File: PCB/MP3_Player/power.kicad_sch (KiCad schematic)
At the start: 18 parts, among them J5 BAT Connector, SW1 Power SW, U2 AP2112K-3.3, U3 BQ24075RGTR, U5 MAX17048G

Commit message: Minor Schematic Changes
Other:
- note added: "GND Test point"
- moved on the sheet: BT1, TP4
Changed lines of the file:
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@@
 	)
 	(rectangle
-		(start 114.3 139.7)
-		(end 129.54 151.13)
+		(start 49.53 152.4)
+		(end 64.77 163.83)
 		(stroke
 			(width 0)
@@
 	(text "Battery BOM Placeholder"
 		(exclude_from_sim no)
-		(at 124.46 154.432 0)
+		(at 57.658 167.386 0)
 		(effects
 			(font
@@
 	(text "For ERC\nIgnore"
 		(exclude_from_sim no)
-		(at 50.546 130.81 0)
+		(at 89.154 130.81 0)
 		(effects
 			(font
@@
 		)
 	)
+	(text "GND Test \npoint"
+		(exclude_from_sim no)
+		(at 108.966 130.81 0)
+		(effects
+			(font
+				(size 1.27 1.27)
+			)
+		)
+	)
 	(text "Power Switch"
 		(exclude_from_sim no)
@@
 	)
 	(no_connect
-		(at 125.73 143.51)
+		(at 60.96 156.21)
 	)
 	(no_connect
@@
 	)
 	(no_connect
-		(at 118.11 143.51)
+		(at 53.34 156.21)
 	)
 	(no_connect
@@
 	(wire
 		(pts
-			(xy 41.91 129.54) (xy 41.91 132.08)
+			(xy 95.25 129.54) (xy 95.25 132.08)
 		)
 		(stroke
@@
 	(wire
 		(pts
-			(xy 101.6 125.73) (xy 101.6 127)
+			(xy 102.87 130.81) (xy 102.87 132.08)
 		)
 		(stroke
@@
 	(symbol
 		(lib_id "power:GND")
-		(at 101.6 127 0)
+		(at 102.87 132.08 0)
 		(unit 1)
 		(body_style 1)
@@
 		(fields_autoplaced yes)
 		(property "Reference" "#PWR057"
-			(at 101.6 133.35 0)
+			(at 102.87 138.43 0)
 			(hide yes)
 			(show_name no)
@@
 		)
 		(property "Value" "GND"
-			(at 101.6 132.08 0)
+			(at 102.87 137.16 0)
 			(hide yes)
 			(show_name no)
@@
 		)
 		(property "Footprint" ""
-			(at 101.6 127 0)
+			(at 102.87 132.08 0)
 			(hide yes)
 			(show_name no)
@@
 		)
 		(property "Datasheet" ""
-			(at 101.6 127 0)
+			(at 102.87 132.08 0)
 			(hide yes)
 			(show_name no)
@@
 		)
 		(property "Description" "Power symbol creates a global label with name \"GND\" , ground"
-			(at 101.6 127 0)
+			(at 102.87 132.08 0)
 			(hide yes)
 			(show_name no)
@@
 	(symbol
 		(lib_id "power:PWR_FLAG")
-		(at 41.91 129.54 0)
+		(at 95.25 129.54 0)
 		(unit 1)
 		(body_style 1)
@@
 		(fields_autoplaced yes)
 		(property "Reference" "#FLG01"
-			(at 41.91 127.635 0)
+			(at 95.25 127.635 0)
 			(hide yes)
 			(show_name no)
@@
 		)
 		(property "Value" "PWR_FLAG"
-			(at 41.91 124.46 0)
+			(at 95.25 124.46 0)
 			(show_name no)
 			(do_not_autoplace no)
@@
 		)
 		(property "Footprint" ""
-			(at 41.91 129.54 0)
+			(at 95.25 129.54 0)
 			(hide yes)
 			(show_name no)
@@
 		)
 		(property "Datasheet" ""
-			(at 41.91 129.54 0)
+			(at 95.25 129.54 0)
 			(hide yes)
 			(show_name no)
@@
 		)
 		(property "Description" "Special symbol for telling ERC where power comes from"
-			(at 41.91 129.54 0)
+			(at 95.25 129.54 0)
 			(hide yes)
 			(show_name no)
@@
 	(symbol
 		(lib_id "Device:Battery_Cell")
-		(at 123.19 143.51 90)
+		(at 58.42 156.21 90)
 		(unit 1)
 		(body_style 1)
@@
 		(dnp no)
 		(property "Reference" "BT1"
-			(at 122.428 147.32 90)
+			(at 57.658 160.02 90)
 			(show_name no)
 			(do_not_autoplace no)
@@
 		)
 		(property "Value" "Battery_Cell"
-			(at 122.3645 148.844 90)
+			(at 57.5945 161.544 90)
 			(show_name no)
 			(do_not_autoplace no)
@@
 		)
 		(property "Footprint" ""
-			(at 121.666 143.51 90)
+			(at 56.896 156.21 90)
 			(hide yes)
 			(show_name no)
@@
 		)
 		(property "Datasheet" ""
-			(at 121.666 143.51 90)
+			(at 56.896 156.21 90)
 			(hide yes)
 			(show_name no)
@@
 		)
 		(property "Description" "Single-cell battery"
-			(at 123.19 143.51 0)
+			(at 58.42 156.21 0)
 			(hide yes)
 			(show_name no)
@@
 		)
 		(property "Sim.Device" "V"
-			(at 123.19 143.51 0)
+			(at 58.42 156.21 0)
 			(hide yes)
 			(show_name no)
@@
 		)
 		(property "Sim.Type" "DC"
-			(at 123.19 143.51 0)
+			(at 58.42 156.21 0)
 			(hide yes)
 			(show_name no)
@@
 		)
 		(property "Sim.Pins" "1=+ 2=-"
-			(at 123.19 143.51 0)
+			(at 58.42 156.21 0)
 			(hide yes)
 			(show_name no)
@@
 		)
 		(property "Mfr. Part Number" ""
-			(at 123.19 143.51 90)
+			(at 58.42 156.21 90)
 			(hide yes)
 			(show_name no)
@@
 	(symbol
 		(lib_id "power:GND")
-		(at 41.91 132.08 0)
+		(at 95.25 132.08 0)
 		(unit 1)
 		(body_style 1)
@@
 		(fields_autoplaced yes)
 		(property "Reference" "#PWR074"
-			(at 41.91 138.43 0)
+			(at 95.25 138.43 0)
 			(hide yes)
 			(show_name no)
@@
 		)
 		(property "Value" "GND"
-			(at 41.91 137.16 0)
+			(at 95.25 137.16 0)
 			(hide yes)
 			(show_name no)
@@
 		)
 		(property "Footprint" ""
-			(at 41.91 132.08 0)
+			(at 95.25 132.08 0)
 			(hide yes)
 			(show_name no)
@@
 		)
 		(property "Datasheet" ""
-			(at 41.91 132.08 0)
+			(at 95.25 132.08 0)
 			(hide yes)
 			(show_name no)
@@
 		)
 		(property "Description" "Power symbol creates a global label with name \"GND\" , ground"
-			(at 41.91 132.08 0)
+			(at 95.25 132.08 0)
 			(hide yes)
 			(show_name no)
@@
 	(symbol
 		(lib_id "Connector:TestPoint")
-		(at 101.6 125.73 0)
+		(at 102.87 130.81 0)
 		(unit 1)
 		(body_style 1)
@@
 		(dnp no)
 		(property "Reference" "TP4"
-			(at 105.283 121.285 0)
+			(at 103.124 122.428 0)
 			(show_name no)
 			(do_not_autoplace no)
@@
 		)
 		(property "Value" "GND"
-			(at 105.283 123.825 0)
+			(at 103.124 124.968 0)
 			(show_name no)
 			(do_not_autoplace no)
@@
 		)
 		(property "Footprint" "Relay_THT:Relay_DPDT_Schrack-RT2-FormC_RM5mm"
-			(at 106.68 125.73 0)
+			(at 107.95 130.81 0)
 			(hide yes)
 			(show_name no)
@@
 		)
 		(property "Datasheet" ""
-			(at 106.68 125.73 0)
+			(at 107.95 130.81 0)
 			(hide yes)
 			(show_name no)
@@
 		)
 		(property "Description" "test point"
-			(at 101.6 125.73 0)
+			(at 102.87 130.81 0)
 			(hide yes)
 			(show_name no)

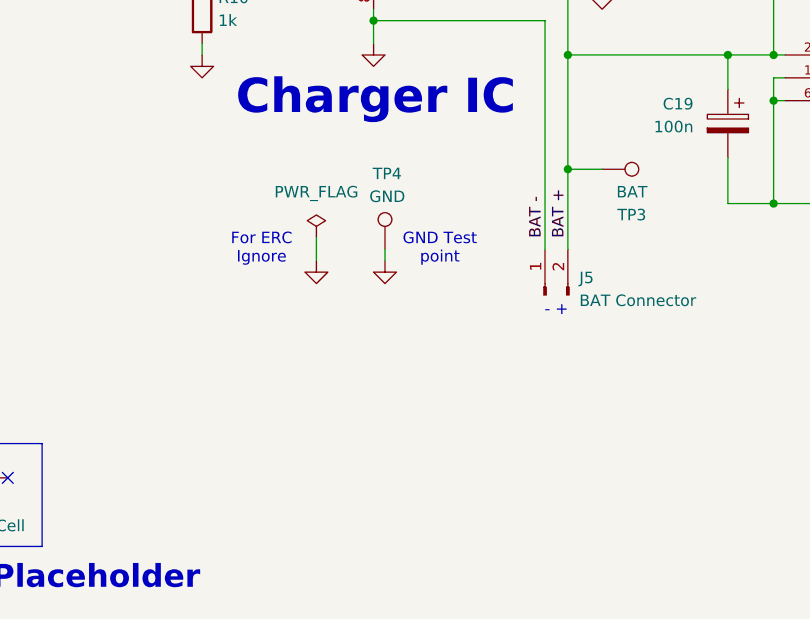
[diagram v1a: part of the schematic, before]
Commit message: Visual Schematic Corrections
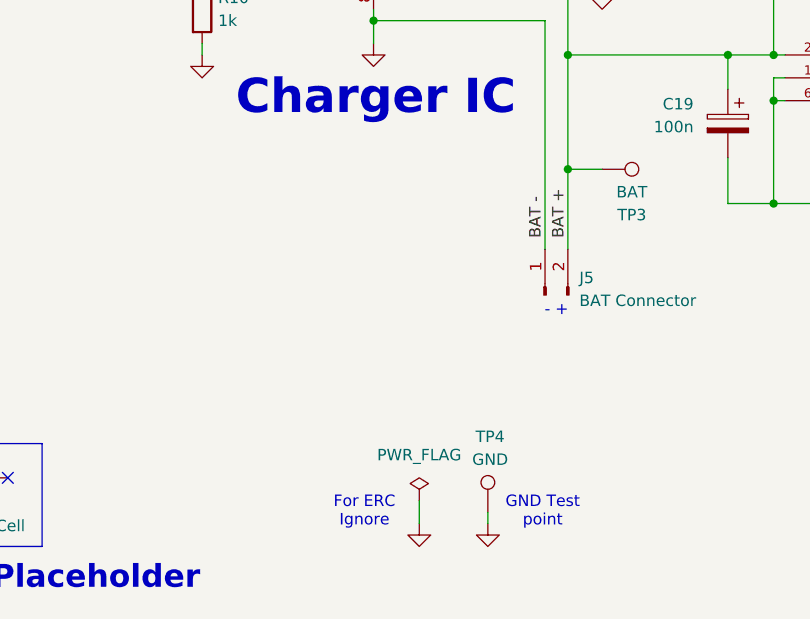
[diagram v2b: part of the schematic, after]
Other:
- moved on the sheet: TP4
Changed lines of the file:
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@@
 	(text "For ERC\nIgnore"
 		(exclude_from_sim no)
-		(at 89.154 130.81 0)
+		(at 100.584 160.02 0)
 		(effects
 			(font
@@
 	(text "GND Test \npoint"
 		(exclude_from_sim no)
-		(at 108.966 130.81 0)
+		(at 120.396 160.02 0)
 		(effects
 			(font
@@
 	(wire
 		(pts
-			(xy 95.25 129.54) (xy 95.25 132.08)
+			(xy 106.68 158.75) (xy 106.68 161.29)
 		)
 		(stroke
@@
 	(wire
 		(pts
-			(xy 102.87 130.81) (xy 102.87 132.08)
+			(xy 114.3 160.02) (xy 114.3 161.29)
 		)
 		(stroke
@@
 	(symbol
 		(lib_id "power:GND")
-		(at 102.87 132.08 0)
+		(at 114.3 161.29 0)
 		(unit 1)
 		(body_style 1)
@@
 		(fields_autoplaced yes)
 		(property "Reference" "#PWR057"
-			(at 102.87 138.43 0)
+			(at 114.3 167.64 0)
 			(hide yes)
 			(show_name no)
@@
 		)
 		(property "Value" "GND"
-			(at 102.87 137.16 0)
+			(at 114.3 166.37 0)
 			(hide yes)
 			(show_name no)
@@
 		)
 		(property "Footprint" ""
-			(at 102.87 132.08 0)
+			(at 114.3 161.29 0)
 			(hide yes)
 			(show_name no)
@@
 		)
 		(property "Datasheet" ""
-			(at 102.87 132.08 0)
+			(at 114.3 161.29 0)
 			(hide yes)
 			(show_name no)
@@
 		)
 		(property "Description" "Power symbol creates a global label with name \"GND\" , ground"
-			(at 102.87 132.08 0)
+			(at 114.3 161.29 0)
 			(hide yes)
 			(show_name no)
@@
 	(symbol
 		(lib_id "power:PWR_FLAG")
-		(at 95.25 129.54 0)
+		(at 106.68 158.75 0)
 		(unit 1)
 		(body_style 1)
@@
 		(fields_autoplaced yes)
 		(property "Reference" "#FLG01"
-			(at 95.25 127.635 0)
+			(at 106.68 156.845 0)
 			(hide yes)
 			(show_name no)
@@
 		)
 		(property "Value" "PWR_FLAG"
-			(at 95.25 124.46 0)
+			(at 106.68 153.67 0)
 			(show_name no)
 			(do_not_autoplace no)
@@
 		)
 		(property "Footprint" ""
-			(at 95.25 129.54 0)
+			(at 106.68 158.75 0)
 			(hide yes)
 			(show_name no)
@@
 		)
 		(property "Datasheet" ""
-			(at 95.25 129.54 0)
+			(at 106.68 158.75 0)
 			(hide yes)
 			(show_name no)
@@
 		)
 		(property "Description" "Special symbol for telling ERC where power comes from"
-			(at 95.25 129.54 0)
+			(at 106.68 158.75 0)
 			(hide yes)
 			(show_name no)
@@
 	(symbol
 		(lib_id "power:GND")
-		(at 95.25 132.08 0)
+		(at 106.68 161.29 0)
 		(unit 1)
 		(body_style 1)
@@
 		(fields_autoplaced yes)
 		(property "Reference" "#PWR074"
-			(at 95.25 138.43 0)
+			(at 106.68 167.64 0)
 			(hide yes)
 			(show_name no)
@@
 		)
 		(property "Value" "GND"
-			(at 95.25 137.16 0)
+			(at 106.68 166.37 0)
 			(hide yes)
 			(show_name no)
@@
 		)
 		(property "Footprint" ""
-			(at 95.25 132.08 0)
+			(at 106.68 161.29 0)
 			(hide yes)
 			(show_name no)
@@
 		)
 		(property "Datasheet" ""
-			(at 95.25 132.08 0)
+			(at 106.68 161.29 0)
 			(hide yes)
 			(show_name no)
@@
 		)
 		(property "Description" "Power symbol creates a global label with name \"GND\" , ground"
-			(at 95.25 132.08 0)
+			(at 106.68 161.29 0)
 			(hide yes)
 			(show_name no)
@@
 	(symbol
 		(lib_id "Connector:TestPoint")
-		(at 102.87 130.81 0)
+		(at 114.3 160.02 0)
 		(unit 1)
 		(body_style 1)
@@
 		(dnp no)
 		(property "Reference" "TP4"
-			(at 103.124 122.428 0)
+			(at 114.554 151.638 0)
 			(show_name no)
 			(do_not_autoplace no)
@@
 		)
 		(property "Value" "GND"
-			(at 103.124 124.968 0)
+			(at 114.554 154.178 0)
 			(show_name no)
 			(do_not_autoplace no)
@@
 		)
 		(property "Footprint" "Relay_THT:Relay_DPDT_Schrack-RT2-FormC_RM5mm"
-			(at 107.95 130.81 0)
+			(at 119.38 160.02 0)
 			(hide yes)
 			(show_name no)
@@
 		)
 		(property "Datasheet" ""
-			(at 107.95 130.81 0)
+			(at 119.38 160.02 0)
 			(hide yes)
 			(show_name no)
@@
 		)
 		(property "Description" "test point"
-			(at 102.87 130.81 0)
+			(at 114.3 160.02 0)
 			(hide yes)
 			(show_name no)

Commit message: Started Making BOM
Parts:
- C14, C17, C18: Mfr. Part # (none) -> CL05A105MQ5NNND; Store URL - Digikey (none) -> https://www.digikey.pt/pt/products/detail/samsung-electro-m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; Store URL - Mouser (none) -> https://pt.mouser.com/en/ProductDetail/Samsung-Electro-Mech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
- C15, C16: Mfr. Part # (none) -> CL10A475KQ8NNNL; Store URL - Digikey (none) -> https://www.digikey.pt/pt/products/detail/samsung-electro-m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; Store URL - Mouser (none) -> https://pt.mouser.com/en/ProductDetail/Samsung-Electro-Mech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
- C19: Mfr. Part # (none) -> CL05B104KP5NNNC; Store URL - Digikey (none) -> https://www.digikey.pt/pt/products/detail/samsung-electro-m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; Store URL - Mouser (none) -> https://pt.mouser.com/en/ProductDetail/Samsung-Electro-Mech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
- TP3, TP4, TP5, TP6: now left out of the parts list

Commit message: Continue Making BOM
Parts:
- R10: Mfr. Part # (none) -> CRCW04021K00FKED; Store URL - Digikey (none) -> https://www.digikey.pt/pt/products/detail/vishay-dale/CRCW0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; Store URL - Mouser (none) -> https://pt.mouser.com/en/ProductDetail/Vishay/CRCW04021K00F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
- R9: Mfr. Part # (none) -> CRCW040210K0FKED; Store URL - Digikey (none) -> https://www.digikey.pt/pt/products/detail/vishay-dale/CRCW0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; Store URL - Mouser (none) -> https://pt.mouser.com/en/ProductDetail/Vishay/CRCW040210K0F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
- SW1: value Power SW -> Toggle Switch; Mfr. Part # (none) -> SWS010-020R12SSA; Store URL - Digikey (none) -> https://www.digikey.pt/pt/products/detail/gct/SWS010-020R12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; Store URL - Mouser (none) -> https://pt.mouser.com/en/ProductDetail/GCT/SWS010-020R12SSA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
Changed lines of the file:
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@@
 			)
 		)
-		(property "Datasheet" ""
+		(property "Datasheet" "https://www.vishay.com/docs/20035/dcrcwe3.pdf"
 			(at 127 96.52 0)
 			(hide yes)
@@
 			)
 		)
-		(property "Description" "Resistor"
+		(property "Description" "0402"
 			(at 127 96.52 0)
 			(hide yes)
@@
 		)
 		(property "Store URL - TME" ""
+			(at 127 96.52 0)
+			(hide yes)
+			(show_name no)
+			(do_not_autoplace no)
+			(effects
+				(font
+					(size 1.27 1.27)
+				)
+			)
+		)
+		(property "Mfr. Part #" "CRCW040210K0FKED"
+			(at 127 96.52 0)
+			(hide yes)
+			(show_name no)
+			(do_not_autoplace no)
+			(effects
+				(font
+					(size 1.27 1.27)
+				)
+			)
+		)
+		(property "Store URL - Digikey" "https://www.digikey.pt/pt/products/detail/vishay-dale/CRCW040210K0FKED/1178121"
+			(at 127 96.52 0)
+			(hide yes)
+			(show_name no)
+			(do_not_autoplace no)
+			(effects
+				(font
+					(size 1.27 1.27)
+				)
+			)
+		)
+		(property "Store URL - Mouser" "https://pt.mouser.com/en/ProductDetail/Vishay/CRCW040210K0FKED?qs=rlE3Te1NifyN3e8vvxacSw%3D%3D"
 			(at 127 96.52 0)
 			(hide yes)
@@
 			)
 		)
-		(property "Value" "Power SW"
+		(property "Value" "Toggle Switch"
 			(at 201.93 72.3899 90)
 			(show_name no)
@@
 			)
 		)
-		(property "Datasheet" ""
+		(property "Datasheet" "https://gct.co/download?type=PDFSpecification&name=sws010-spec.pdf"
 			(at 204.47 71.12 0)
 			(hide yes)
@@
 		)
 		(property "Store URL - TME" ""
+			(at 196.85 71.12 90)
+			(hide yes)
+			(show_name no)
+			(do_not_autoplace no)
+			(effects
+				(font
+					(size 1.27 1.27)
+				)
+			)
+		)
+		(property "Mfr. Part #" "SWS010-020R12SSA"
+			(at 196.85 71.12 90)
+			(hide yes)
+			(show_name no)
+			(do_not_autoplace no)
+			(effects
+				(font
+					(size 1.27 1.27)
+				)
+			)
+		)
+		(property "Store URL - Digikey" "https://www.digikey.pt/pt/products/detail/gct/SWS010-020R12SSA/29426304"
+			(at 196.85 71.12 90)
+			(hide yes)
+			(show_name no)
+			(do_not_autoplace no)
+			(effects
+				(font
+					(size 1.27 1.27)
+				)
+			)
+		)
+		(property "Store URL - Mouser" "https://pt.mouser.com/en/ProductDetail/GCT/SWS010-020R12SSA?qs=Naspt24KZtmuNo3rehdP0w%3D%3D"
 			(at 196.85 71.12 90)
 			(hide yes)
@@
 			)
 		)
-		(property "Datasheet" ""
+		(property "Datasheet" "https://www.vishay.com/docs/20035/dcrcwe3.pdf"
 			(at 82.55 104.14 0)
 			(hide yes)
@@
 			)
 		)
-		(property "Description" "Resistor"
+		(property "Description" "0402"
 			(at 82.55 104.14 0)
 			(hide yes)
@@
 			(at 82.55 104.14 0)
 			(hide yes)
+			(show_name no)
+			(do_not_autoplace no)
+			(effects
+				(font
+					(size 1.27 1.27)
+				)
+			)
+		)
+		(property "Mfr. Part #" "CRCW04021K00FKED"
+			(at 82.55 104.14 0)
+			(hide yes)
+			(show_name no)
+			(do_not_autoplace no)
+			(effects
+				(font
+					(size 1.27 1.27)
+				)
+			)
+		)
+		(property "Store URL - Digikey" "https://www.digikey.pt/pt/products/detail/vishay-dale/CRCW04021K00FKED/1178007"
+			(at 82.55 104.14 0)
+			(hide yes)
+			(show_name no)
+			(do_not_autoplace no)
+			(effects
+				(font
+					(size 1.27 1.27)
+				)
+			)
+		)
+		(property "Store URL - Mouser" "https://pt.mouser.com/en/ProductDetail/Vishay/CRCW04021K00FKED?qs=YX%252BK5oaHNYqQ2WK%252BIAW12A%3D%3D"
+			(at 82.55 104.14 0)
+			(hide yes)

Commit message: Finished BOM; Started Footprint assignment
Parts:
- BT1: footprint (none) -> N/A; Store URL - Digikey (none) -> N/A; Store URL - Mouser (none) -> N/A
- C14, C17, C18, C19, R10, R9: footprint (none) -> Capacitor_SMD:C_0402_1005Metric
- C15, C16: footprint (none) -> Capacitor_SMD:C_0603_1608Metric
- J5: Mfr. Part # (none) -> S2B-PH-SM4-TB; Store URL - Digikey (none) -> https://www.digikey.pt/pt/products/detail/jst-sales-america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; Store URL - Mouser (none) -> http://pt.mouser.com/en/ProductDetail/JST-Commercial/S2B-PH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
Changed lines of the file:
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@@
 			)
 		)
-		(property "Datasheet" ""
+		(property "Datasheet" "https://www.jst-mfg.com/product/pdf/eng/ePH.pdf"
 			(at 120.65 135.89 0)
 			(hide yes)
@@
 			)
 		)
-		(property "Description" "Generic connector, single row, 01x02, script generated"
+		(property "Description" "JST 2.0 PH"
 			(at 120.65 135.89 0)
 			(hide yes)
@@
 			)
 		)
+		(property "Mfr. Part #" "S2B-PH-SM4-TB"
+			(at 120.65 135.89 90)
+			(hide yes)
+			(show_name no)
+			(do_not_autoplace no)
+			(effects
+				(font
+					(size 1.27 1.27)
+				)
+			)
+		)
+		(property "Store URL - Digikey" "https://www.digikey.pt/pt/products/detail/jst-sales-america-inc/S2B-PH-SM4-TB/926655?s=N4IgjCBcoGwJxVAYygMwIYBsDOBTANCAPZQDaIALAAxwUBMVIAuoQA4AuUIAyuwE4BLAHYBzEAF9CADimIQKSBhwFiZcHTABmOjGZtOkHv2FjJ4OFITR5aLHkIlI5RkzMBaCnIVL7qpyE0AdnpmcTM6NQArbHYAAjoAOipY1gALUKA"
+			(at 120.65 135.89 90)
+			(hide yes)
+			(show_name no)
+			(do_not_autoplace no)
+			(effects
+				(font
+					(size 1.27 1.27)
+				)
+			)
+		)
+		(property "Store URL - Mouser" "http://pt.mouser.com/en/ProductDetail/JST-Commercial/S2B-PH-SM4-TBLFSN?qs=QpmGXVUTftGPIOdg%2F2bstg%3D%3D"
+			(at 120.65 135.89 90)
+			(hide yes)
+			(show_name no)
+			(do_not_autoplace no)
+			(effects
+				(font
+					(size 1.27 1.27)
+				)
+			)
+		)
 		(pin "1"
 		)
@@
 			)
 		)
-		(property "Footprint" ""
+		(property "Footprint" "Capacitor_SMD:C_0603_1608Metric"
 			(at 132.08 85.3948 0)
 			(hide yes)
@@
 			)
 		)
-		(property "Footprint" ""
+		(property "Footprint" "Capacitor_SMD:C_0402_1005Metric"
 			(at 140.0048 120.65 0)
 			(hide yes)
@@
 			)
 		)
-		(property "Footprint" ""
+		(property "Footprint" "Capacitor_SMD:C_0402_1005Metric"
 			(at 94.9452 63.5 0)
 			(hide yes)
@@
 			)
 		)
-		(property "Footprint" ""
+		(property "Footprint" "Capacitor_SMD:C_0402_1005Metric"
 			(at 125.222 96.52 90)
 			(hide yes)
@@
 			)
 		)
-		(property "Footprint" ""
+		(property "Footprint" "Capacitor_SMD:C_0402_1005Metric"
 			(at 187.6552 86.36 0)
 			(hide yes)
@@
 			)
 		)
-		(property "Footprint" ""
+		(property "Footprint" "N/A"
 			(at 56.896 156.21 90)
 			(hide yes)
@@
 			)
 		)
-		(property "Description" "Single-cell battery"
+		(property "Description" ""
 			(at 58.42 156.21 0)
 			(hide yes)
@@
 			)
 		)
+		(property "Store URL - Digikey" "N/A"
+			(at 58.42 156.21 90)
+			(hide yes)
+			(show_name no)
+			(do_not_autoplace no)
+			(effects
+				(font
+					(size 1.27 1.27)
+				)
+			)
+		)
+		(property "Store URL - Mouser" "N/A"
+			(at 58.42 156.21 90)
+			(hide yes)
+			(show_name no)
+			(do_not_autoplace no)
+			(effects
+				(font
+					(size 1.27 1.27)
+				)
+			)
+		)
 		(pin "1"
 		)
@@
 			)
 		)
-		(property "Footprint" ""
+		(property "Footprint" "Capacitor_SMD:C_0402_1005Metric"
 			(at 80.772 104.14 90)
 			(hide yes)
@@
 			)
 		)
-		(property "Footprint" ""
+		(property "Footprint" "Capacitor_SMD:C_0603_1608Metric"
 			(at 141.9352 87.63 0)
 			(hide yes)
@@
 			)
 		)
-		(property "Footprint" ""
+		(property "Footprint" "Capacitor_SMD:C_0402_1005Metric"
 			(at 155.9052 87.63 0)
 			(hide yes)

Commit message: Footprint Assingment
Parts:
- R10, R9: footprint Capacitor_SMD:C_0402_1005Metric -> Resistor_SMD:R_0402_1005Metric
- TP3, TP4, TP5, TP6: footprint Relay_THT:Relay_DPDT_Schrack-RT2-FormC_RM5mm -> TestPoint:TestPoint_Pad_D1.5mm
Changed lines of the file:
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@@
 			)
 		)
-		(property "Footprint" "Relay_THT:Relay_DPDT_Schrack-RT2-FormC_RM5mm"
+		(property "Footprint" "TestPoint:TestPoint_Pad_D1.5mm"
 			(at 201.93 81.28 0)
 			(hide yes)
@@
 			)
 		)
-		(property "Footprint" "Relay_THT:Relay_DPDT_Schrack-RT2-FormC_RM5mm"
+		(property "Footprint" "TestPoint:TestPoint_Pad_D1.5mm"
 			(at 146.05 78.74 0)
 			(hide yes)
@@
 			)
 		)
-		(property "Footprint" "Relay_THT:Relay_DPDT_Schrack-RT2-FormC_RM5mm"
+		(property "Footprint" "TestPoint:TestPoint_Pad_D1.5mm"
 			(at 127 127 0)
 			(hide yes)
@@
 			)
 		)
-		(property "Footprint" "Capacitor_SMD:C_0402_1005Metric"
+		(property "Footprint" "Resistor_SMD:R_0402_1005Metric"
 			(at 125.222 96.52 90)
 			(hide yes)
@@
 			)
 		)
-		(property "Footprint" "Capacitor_SMD:C_0402_1005Metric"
+		(property "Footprint" "Resistor_SMD:R_0402_1005Metric"
 			(at 80.772 104.14 90)
 			(hide yes)
@@
 			)
 		)
-		(property "Footprint" "Relay_THT:Relay_DPDT_Schrack-RT2-FormC_RM5mm"
+		(property "Footprint" "TestPoint:TestPoint_Pad_D1.5mm"
 			(at 119.38 160.02 0)
 			(hide yes)

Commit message: Footprint Assignment
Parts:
- SW1: footprint (none) -> Button_Switch_SMD:SW_SPDT_CK_JS102011SAQN
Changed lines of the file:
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@@
 			)
 		)
-		(property "Footprint" ""
+		(property "Footprint" "Button_Switch_SMD:SW_SPDT_CK_JS102011SAQN"
 			(at 196.85 71.12 0)
 			(hide yes)

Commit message: Footprint Assingment Complete
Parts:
- J5: footprint (none) -> Connector_JST:JST_PH_S2B-PH-SM4-TB_1x02-1MP_P2.00mm_Horizontal
- TP3, TP4, TP5, TP6: footprint TestPoint:TestPoint_Pad_D1.5mm -> TestPoint:TestPoint_Pad_D1.0mm
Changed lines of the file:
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@@
 			)
 		)
-		(property "Footprint" ""
+		(property "Footprint" "Connector_JST:JST_PH_S2B-PH-SM4-TB_1x02-1MP_P2.00mm_Horizontal"
 			(at 120.65 135.89 0)
 			(hide yes)
@@
 			)
 		)
-		(property "Footprint" "TestPoint:TestPoint_Pad_D1.5mm"
+		(property "Footprint" "TestPoint:TestPoint_Pad_D1.0mm"
 			(at 201.93 81.28 0)
 			(hide yes)
@@
 			)
 		)
-		(property "Footprint" "TestPoint:TestPoint_Pad_D1.5mm"
+		(property "Footprint" "TestPoint:TestPoint_Pad_D1.0mm"
 			(at 146.05 78.74 0)
 			(hide yes)
@@
 			)
 		)
-		(property "Footprint" "TestPoint:TestPoint_Pad_D1.5mm"
+		(property "Footprint" "TestPoint:TestPoint_Pad_D1.0mm"
 			(at 127 127 0)
 			(hide yes)
@@
 			)
 		)
-		(property "Footprint" "TestPoint:TestPoint_Pad_D1.5mm"
+		(property "Footprint" "TestPoint:TestPoint_Pad_D1.0mm"
 			(at 119.38 160.02 0)
 			(hide yes)
